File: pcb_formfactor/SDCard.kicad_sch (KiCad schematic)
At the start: 8 parts, among them J3 SDCARD_DM3AT-SF-PEJM5

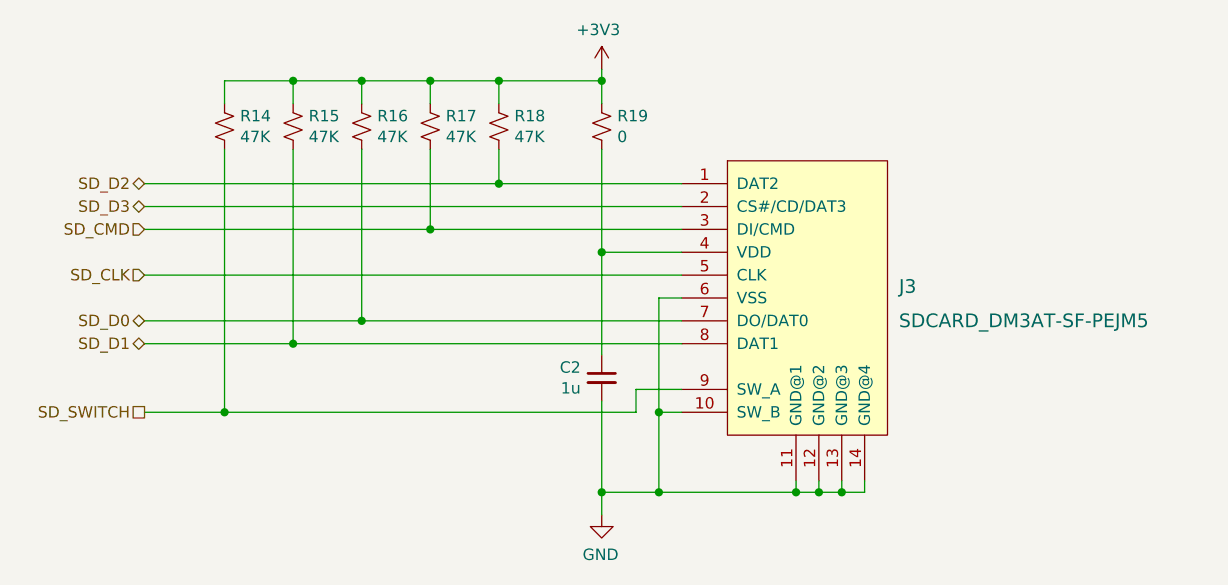
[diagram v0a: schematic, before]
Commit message: Add diode OR, add clock series R
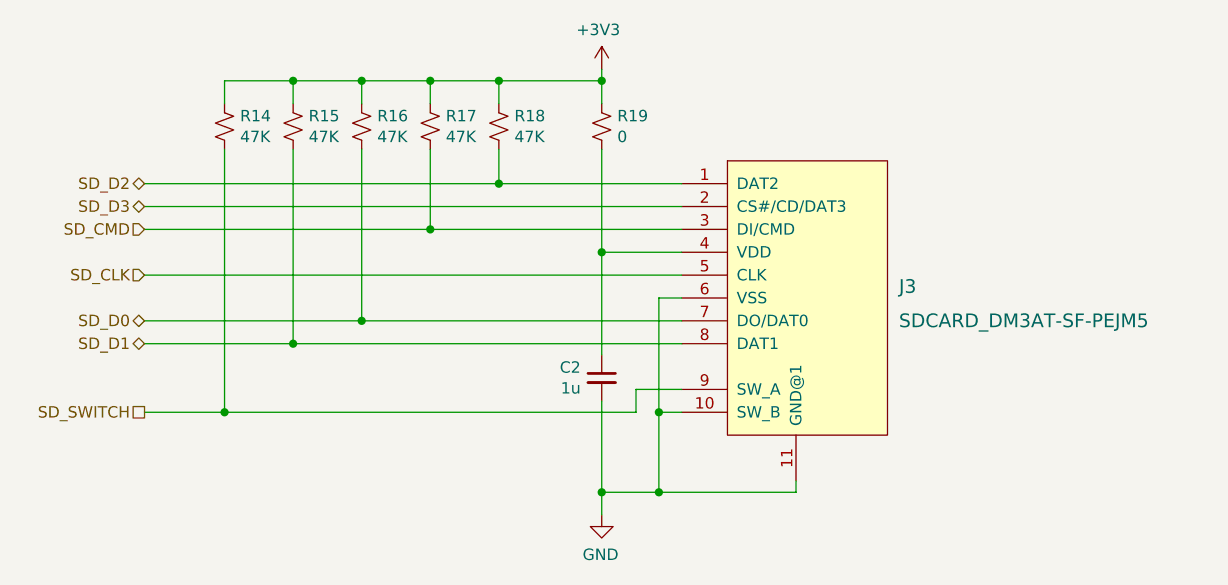
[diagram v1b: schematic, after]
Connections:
- net GND: no longer J3.12 (GND@2), J3.13 (GND@3), J3.14 (GND@4)
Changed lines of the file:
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@@
   (junction (at 119.38 87.63) (diameter 0) (color 0 0 0 0)
   )
-  (junction (at 162.56 116.84) (diameter 0) (color 0 0 0 0)
-  )
   (junction (at 104.14 100.33) (diameter 0) (color 0 0 0 0)
   )
-  (junction (at 160.02 116.84) (diameter 0) (color 0 0 0 0)
-  )
   (junction (at 138.43 71.12) (diameter 0) (color 0 0 0 0)
   )
@@
   (junction (at 119.38 71.12) (diameter 0) (color 0 0 0 0)
   )
-  (junction (at 165.1 116.84) (diameter 0) (color 0 0 0 0)
-  )
   (junction (at 111.76 71.12) (diameter 0) (color 0 0 0 0)
   )
@@
     (stroke (width 0) (type default) (color 0 0 0 0))
   )
-  (wire (pts (xy 162.56 116.84) (xy 165.1 116.84))
-    (stroke (width 0) (type default) (color 0 0 0 0))
-  )
   (wire (pts (xy 138.43 101.6) (xy 138.43 90.17))
     (stroke (width 0) (type default) (color 0 0 0 0))
@@
     (stroke (width 0) (type default) (color 0 0 0 0))
   )
-  (wire (pts (xy 167.64 115.57) (xy 167.64 116.84))
-    (stroke (width 0) (type default) (color 0 0 0 0))
-  )
   (wire (pts (xy 111.76 78.74) (xy 111.76 97.79))
     (stroke (width 0) (type default) (color 0 0 0 0))
@@
     (stroke (width 0) (type default) (color 0 0 0 0))
   )
-  (wire (pts (xy 165.1 115.57) (xy 165.1 116.84))
-    (stroke (width 0) (type default) (color 0 0 0 0))
-  )
-  (wire (pts (xy 162.56 115.57) (xy 162.56 116.84))
-    (stroke (width 0) (type default) (color 0 0 0 0))
-  )
   (wire (pts (xy 87.63 82.55) (xy 127 82.55))
     (stroke (width 0) (type default) (color 0 0 0 0))
@@
   )
   (wire (pts (xy 147.32 87.63) (xy 119.38 87.63))
-    (stroke (width 0) (type default) (color 0 0 0 0))
-  )
-  (wire (pts (xy 165.1 116.84) (xy 167.64 116.84))
-    (stroke (width 0) (type default) (color 0 0 0 0))
-  )
-  (wire (pts (xy 160.02 116.84) (xy 162.56 116.84))
     (stroke (width 0) (type default) (color 0 0 0 0))
   )
@@
     (pin "10")
     (pin "11")
-    (pin "12")
-    (pin "13")
-    (pin "14")
     (pin "2")
     (pin "3")
